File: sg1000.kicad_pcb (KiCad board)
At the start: 2 copper layers, 32 parts, among them CN01 Conn_01x07_Female, SW1 Pause Key, U10 PLCCZ80, U11 AS6C62256-DIP, U12 TMS9918A, U13 74LS139, U16 74LS32, U18 74LS257, U21 74LS257, U3 SN76489AN

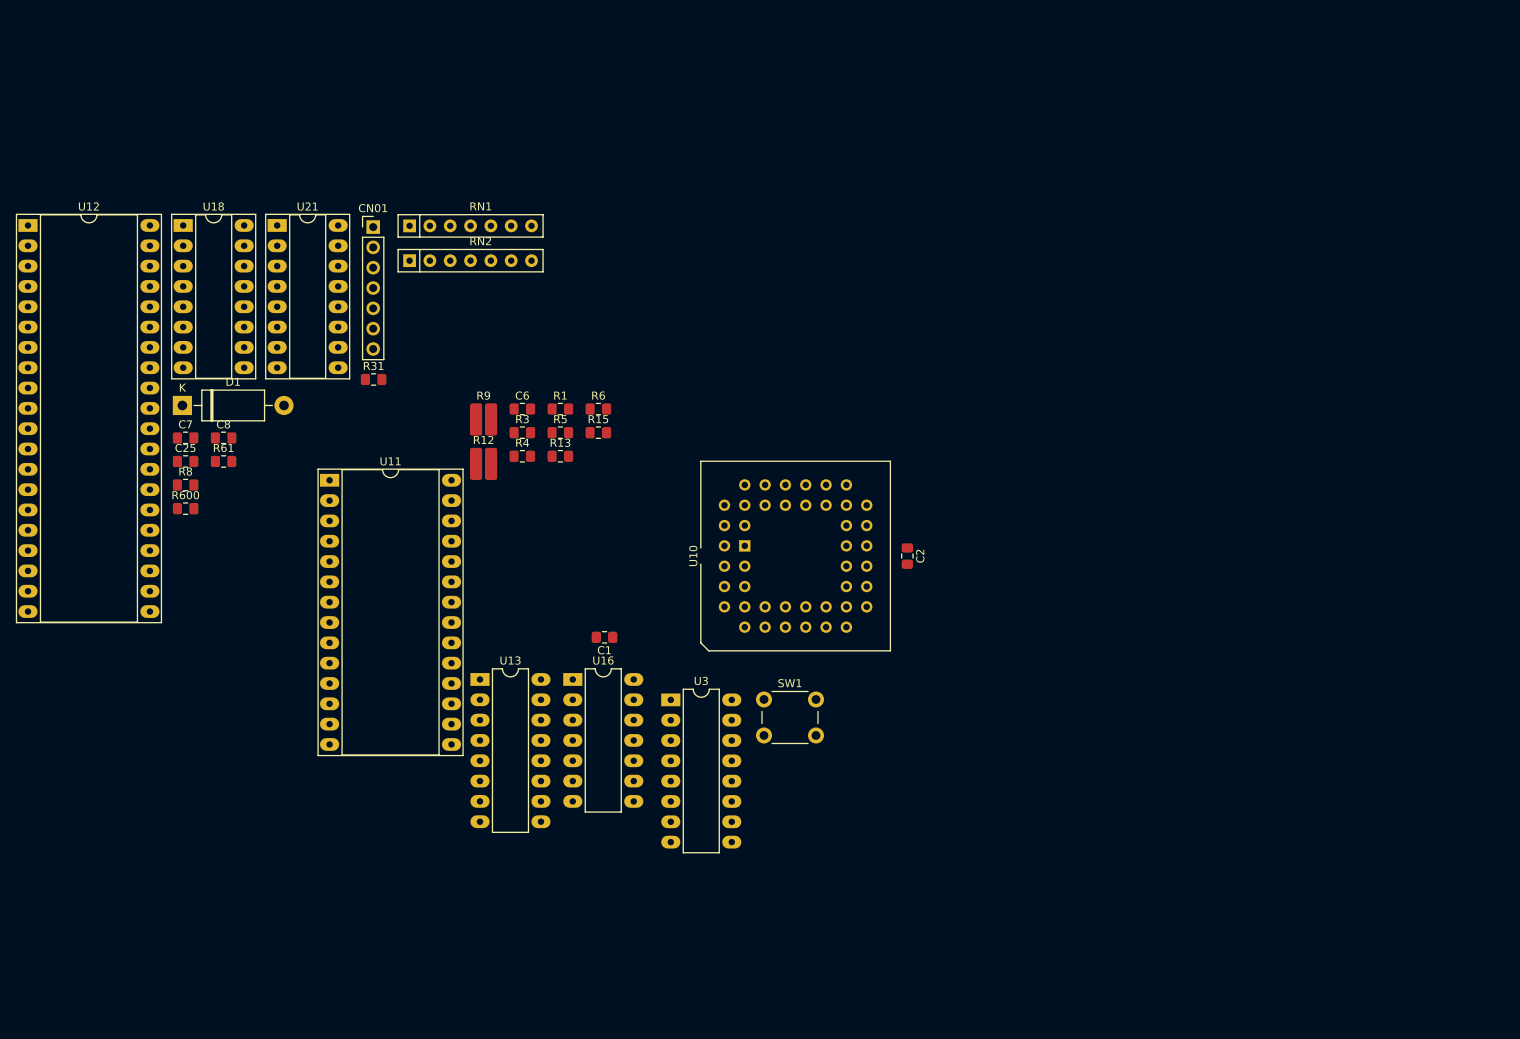
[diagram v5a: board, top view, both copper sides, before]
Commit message: Cart slot symbol
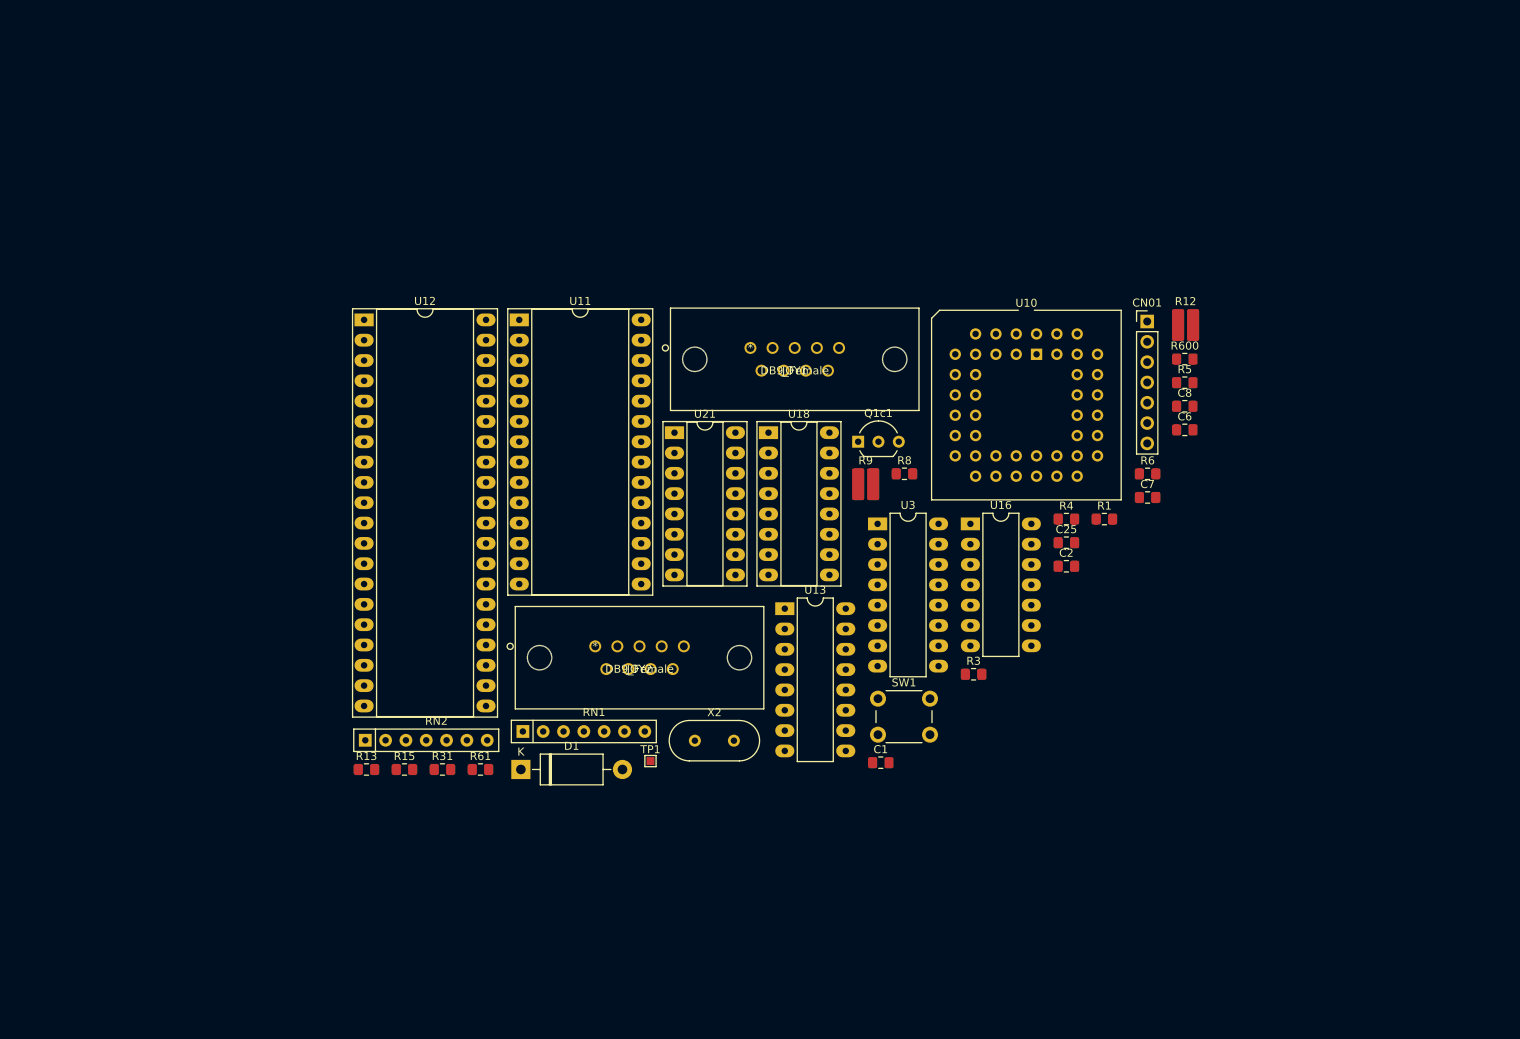
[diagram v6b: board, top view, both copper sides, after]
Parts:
- added JOY1: DB9_Female, LeadedSolder:A-DS 09 A-KG-T2S, F.Cu at (127.7, 64.2)
- added JOY2: DB9_Female, LeadedSolder:A-DS 09 A-KG-T2S, F.Cu at (108.3, 101.5)
- added Q1c1: 2n3906, Package_TO_SOT_THT:TO-92_Inline_Wide, F.Cu at (141.2, 75.9)
- added TP1: TestPoint, TestPoint:TestPoint_Pad_1.0x1.0mm, F.Cu at (115.2, 115.8)
- added X2: 10.73863MHz, Crystal:Crystal_HC49-U_Vertical, F.Cu at (120.8, 113.2)
- moved R600 126.3 mm to (182.0, 65.5)
- moved C7 120.5 mm to (177.3, 82.8)
- moved C8 120.2 mm to (182.0, 71.5)
- moved C25 110.6 mm to (167.2, 88.5)
- moved CN01 97.5 mm to (177.3, 60.9)
- moved R8 89.9 mm to (147.0, 79.9)
- moved R12 89.4 mm to (182.1, 61.3)
- moved C6 82.8 mm to (182.0, 74.4)
- moved R5 78.3 mm to (182.0, 68.5)
- moved U18 77.6 mm to (130.0, 74.8)
- moved R1 69.4 mm to (171.9, 85.5)
- moved R6 69.1 mm to (177.3, 79.9)
- moved R4 68.5 mm to (167.2, 85.5)
- moved RN1 64.8 mm to (99.3, 112.1)
- moved R3 64.0 mm to (155.6, 105.0)
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
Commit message: KiCad6 + VRAM
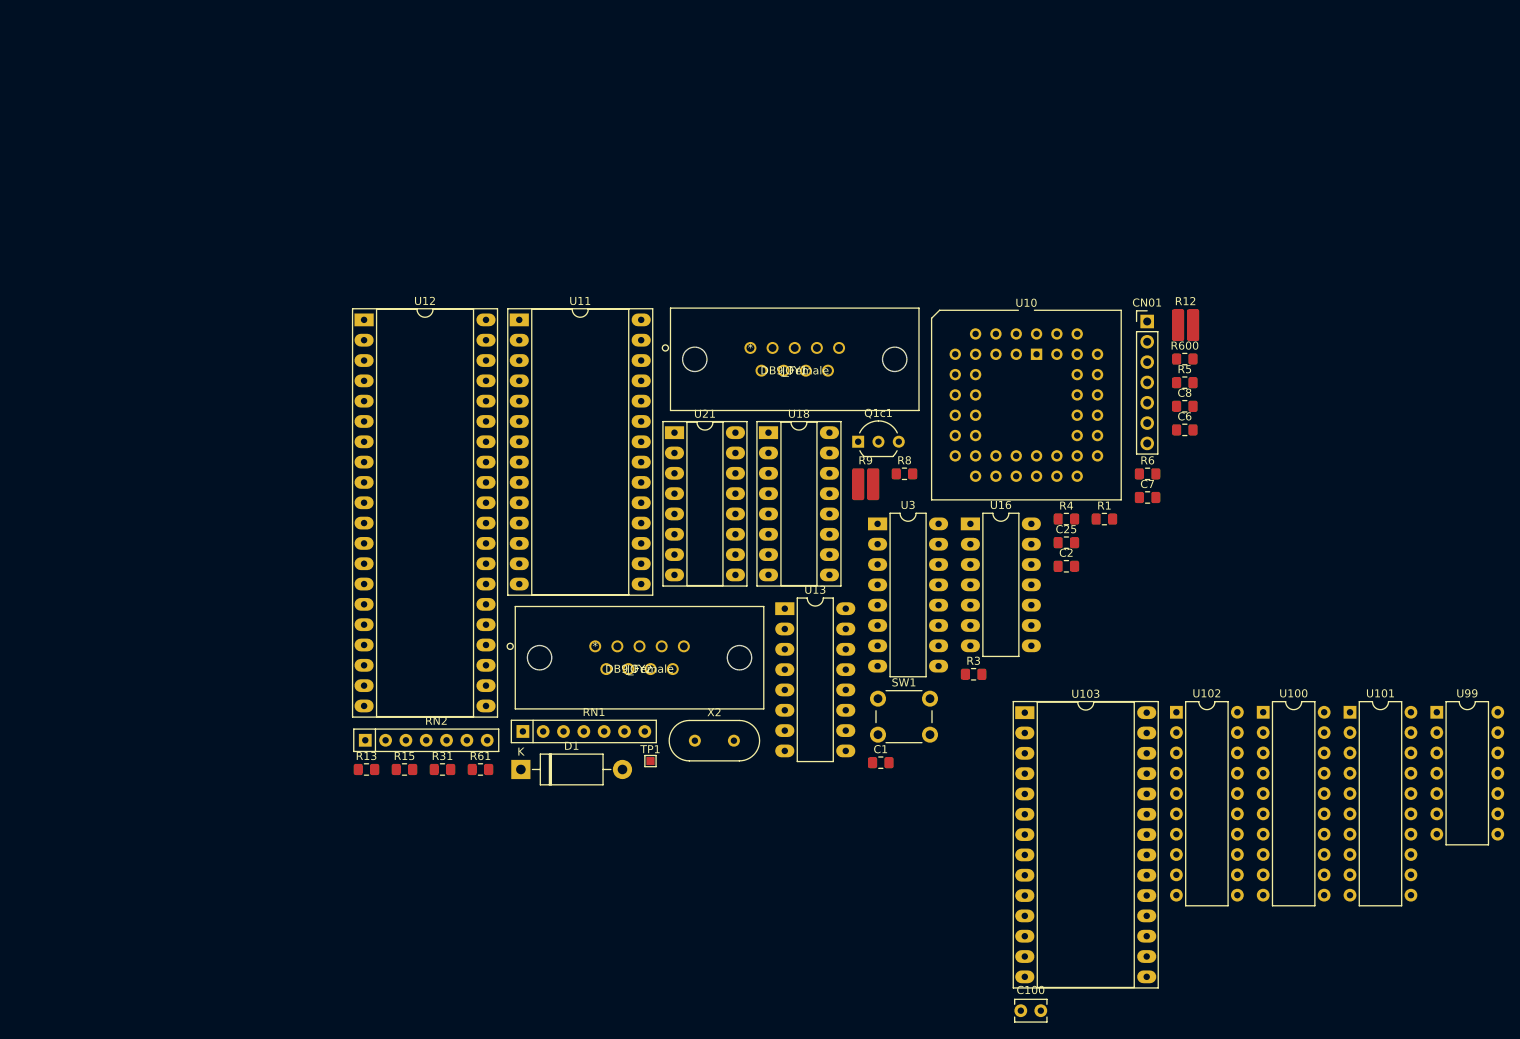
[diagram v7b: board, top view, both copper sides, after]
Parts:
- added C100: 0.1µF, Capacitor_THT:C_Disc_D3.8mm_W2.6mm_P2.50mm, F.Cu at (161.5, 147.0)
- added U100: 74HCT574, Package_DIP:DIP-20_W7.62mm, F.Cu at (191.8, 109.7)
- added U101: 74HCT574, Package_DIP:DIP-20_W7.62mm, F.Cu at (202.7, 109.7)
- added U102: 74HCT574, Package_DIP:DIP-20_W7.62mm, F.Cu at (180.9, 109.7)
- added U103: AS6C62256-DIP, Package_DIP:DIP-28_W15.24mm_Socket_LongPads, F.Cu at (162.0, 109.8)
- added U99: 74HCT04, Package_DIP:DIP-14_W7.62mm, F.Cu at (213.5, 109.7)
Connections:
- net /~CS_PSG renamed /~{CS_PSG}
- net /~CS_WRAM renamed /~{CS_WRAM}
- net /~EXM1 renamed /~{EXM1}
- net /~EXM2 renamed /~{EXM2}
- net /~HALT renamed /~{HALT}
- net /~INT renamed /~{INT}
- net /~IORQ renamed /~{IORQ}
- net /~JOY_SEL renamed /~{JOY_SEL}
- net /~KB_SEL renamed /~{KB_SEL}
- net /~M1 renamed /~{M1}
- net /~MREQ renamed /~{MREQ}
- net /~NMI renamed /~{NMI}
- net /~RD renamed /~{RD}
- net /~RESET renamed /~{RESET}
- net /~RFSH renamed /~{RFSH}
- net /~VDP_RD renamed /~{VDP_RD}
- net /~VDP_WR renamed /~{VDP_WR}
- net /~WAIT renamed /~{WAIT}
- net /~WR renamed /~{WR}
- JOY1 pad 5: Net-(JOY1-Pad5) -> unconnected-(JOY1-Pad5)
- JOY2 pad 5: Net-(JOY2-Pad5) -> unconnected-(JOY2-Pad5)
- U10 pad 27: Net-(U10-Pad27) -> unconnected-(U10-Pad27)
- U12 pad 1: Net-(U12-Pad1) -> /~{VDP_RAS}
- U12 pad 10: Net-(U12-Pad10) -> /AD0
- U12 pad 11: Net-(U12-Pad11) -> /VDP_R~{W}
- U12 pad 2: Net-(U12-Pad2) -> /~{VDP_CAS}
- U12 pad 25: Net-(U12-Pad25) -> /VD7
- U12 pad 26: Net-(U12-Pad26) -> /VD6
- U12 pad 27: Net-(U12-Pad27) -> /VD5
- U12 pad 28: Net-(U12-Pad28) -> /VD4
- U12 pad 29: Net-(U12-Pad29) -> /VD3
- U12 pad 3: Net-(U12-Pad3) -> /AD7
- U12 pad 30: Net-(U12-Pad30) -> /VD2
- U12 pad 31: Net-(U12-Pad31) -> /VD1
- U12 pad 32: Net-(U12-Pad32) -> /VD0
- U12 pad 35: Net-(U12-Pad35) -> unconnected-(U12-Pad35)
- U12 pad 37: Net-(U12-Pad37) -> unconnected-(U12-Pad37)
- U12 pad 4: Net-(U12-Pad4) -> /AD6
- U12 pad 5: Net-(U12-Pad5) -> /AD5
- U12 pad 6: Net-(U12-Pad6) -> /AD4
- U12 pad 7: Net-(U12-Pad7) -> /AD3
- U12 pad 8: Net-(U12-Pad8) -> /AD2
- U12 pad 9: Net-(U12-Pad9) -> /AD1
- U13 pad 12: Net-(U13-Pad12) -> unconnected-(U13-Pad12)
- U13 pad 4: Net-(U13-Pad4) -> unconnected-(U13-Pad4)
- U13 pad 5: Net-(U13-Pad5) -> unconnected-(U13-Pad5)
- U21 pad 10: Net-(U21-Pad10) -> unconnected-(U21-Pad10)
- U21 pad 13: Net-(U21-Pad13) -> unconnected-(U21-Pad13)
- U21 pad 6: Net-(U21-Pad6) -> unconnected-(U21-Pad6)
- U3 pad 9: Net-(U3-Pad9) -> unconnected-(U3-Pad9)
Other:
- net class Default removed

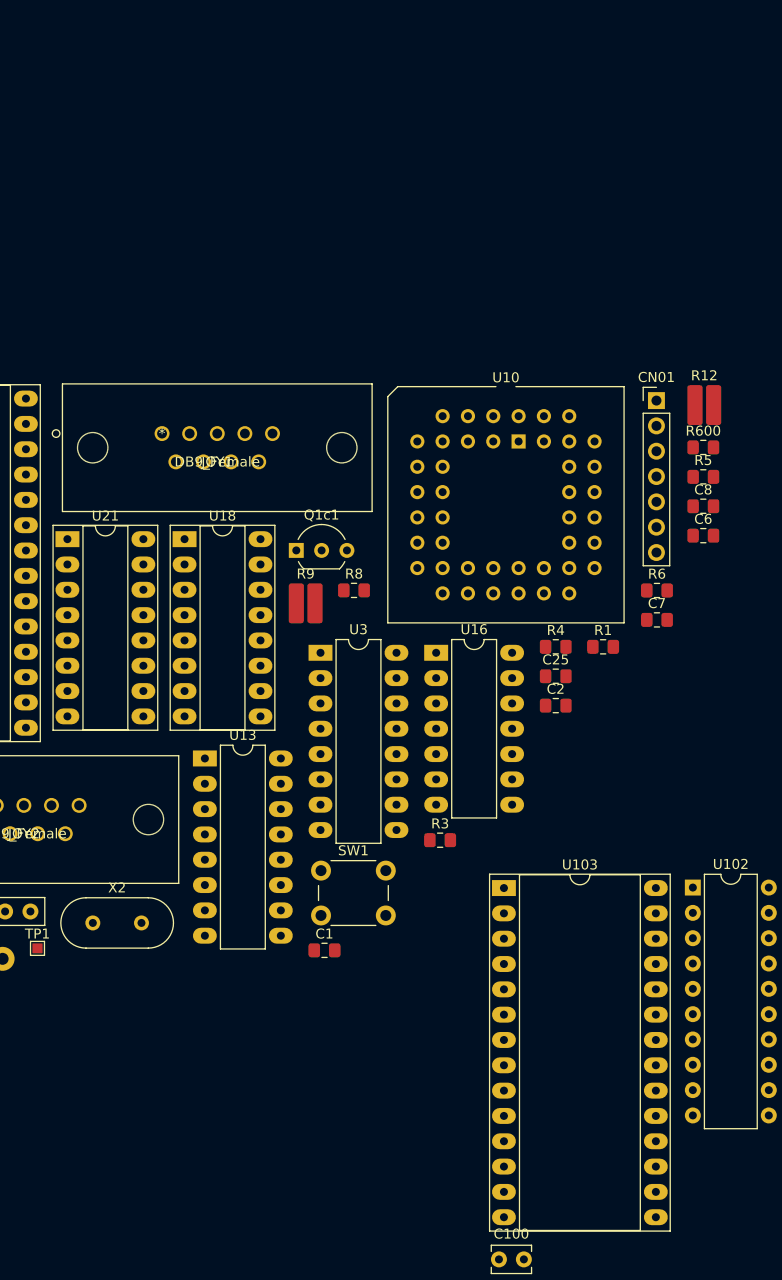
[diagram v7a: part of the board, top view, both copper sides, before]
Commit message: Power supply, cart slot
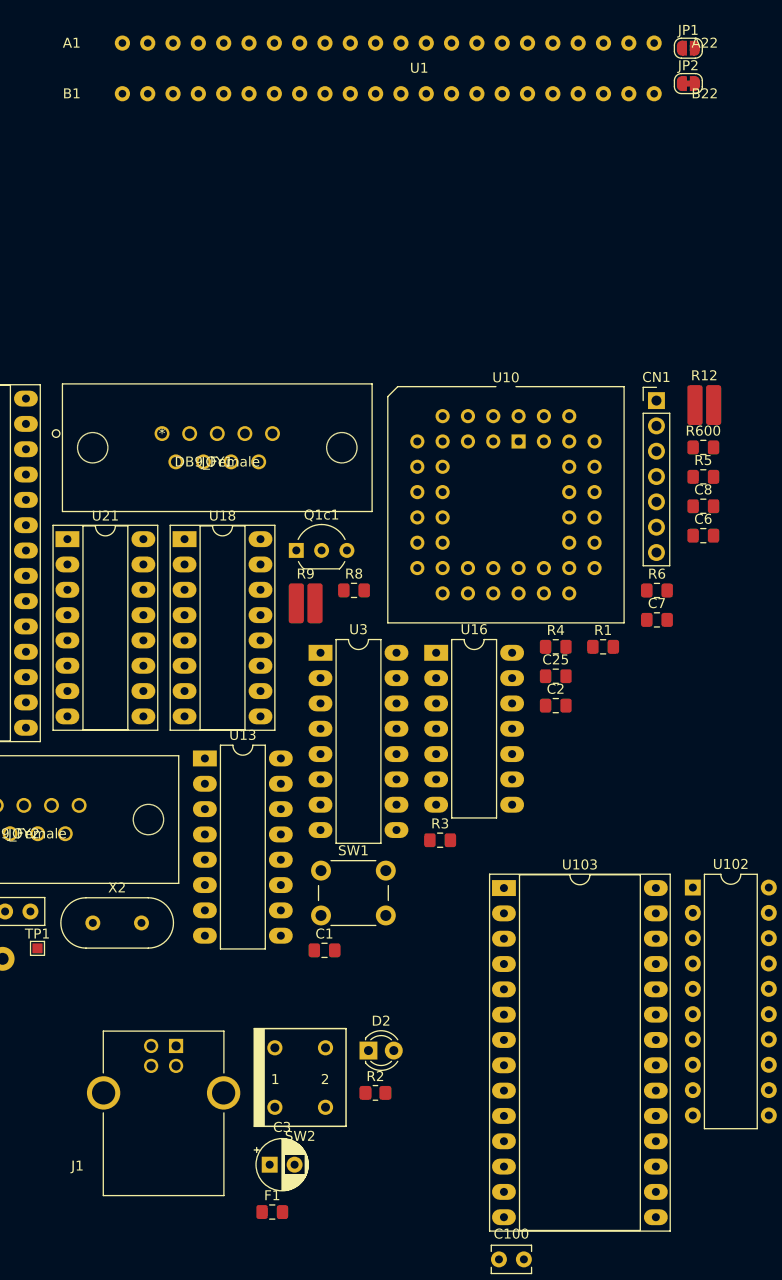
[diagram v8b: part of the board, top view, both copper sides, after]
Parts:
- added C3: 22µF, Capacitor_THT:CP_Radial_D5.0mm_P2.50mm, F.Cu at (138.5, 137.5)
- added D2: LED, LED_THT:LED_D3.0mm, F.Cu at (148.4, 126.0)
- added F1: 2A, Fuse:Fuse_0805_2012Metric_Pad1.15x1.40mm_HandSolder, F.Cu at (138.8, 142.2)
- added J1: USB-B1HSB6, USB-B1HSB6:OST_USB-B1HSB6, F.Cu at (127.9, 130.3)
- added JP1: SolderJumper_2_Open, Jumper:SolderJumper-2_P1.3mm_Open_RoundedPad1.0x1.5mm, F.Cu at (180.5, 25.5)
- added JP2: SolderJumper_2_Bridged, Jumper:SolderJumper-2_P1.3mm_Bridged_RoundedPad1.0x1.5mm, F.Cu at (180.5, 29.1)
- added R2: 560Ω, Resistor_SMD:R_0805_2012Metric_Pad1.20x1.40mm_HandSolder, F.Cu at (149.1, 130.3)
- added SW2: Power Toggle, LeakyChips:PVA1_Switch, F.Cu at (141.6, 128.9)
- added U1: SG-1000-Cart, LeadedSolder:SG1000_Cart, F.Cu at (150.4, 27.5)
- renumbered CN01 to CN1
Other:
- board text added: "TODO: Figure out the keepout for an entire cartridge"
